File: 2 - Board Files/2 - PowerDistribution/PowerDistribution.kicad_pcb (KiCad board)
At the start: 6 copper layers, 100.1 x 100.1 mm, 64 parts, among them J201 Battery Input, J202 Battery Balance Connector, J301 Conn_02x15_Counter_Clockwise, U201 MAX40056F, U202 MAX40056F, U501 AOZ6605PI

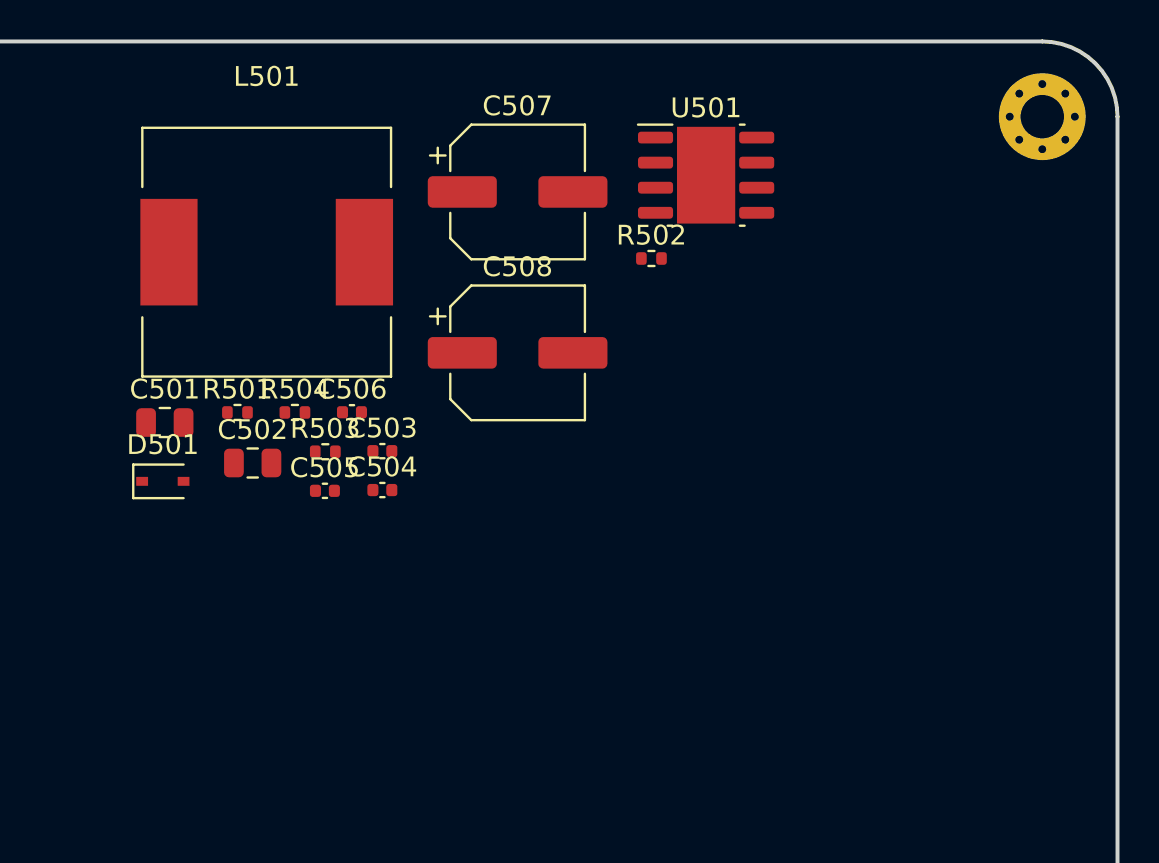
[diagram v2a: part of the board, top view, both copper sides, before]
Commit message: Switching regulator changes
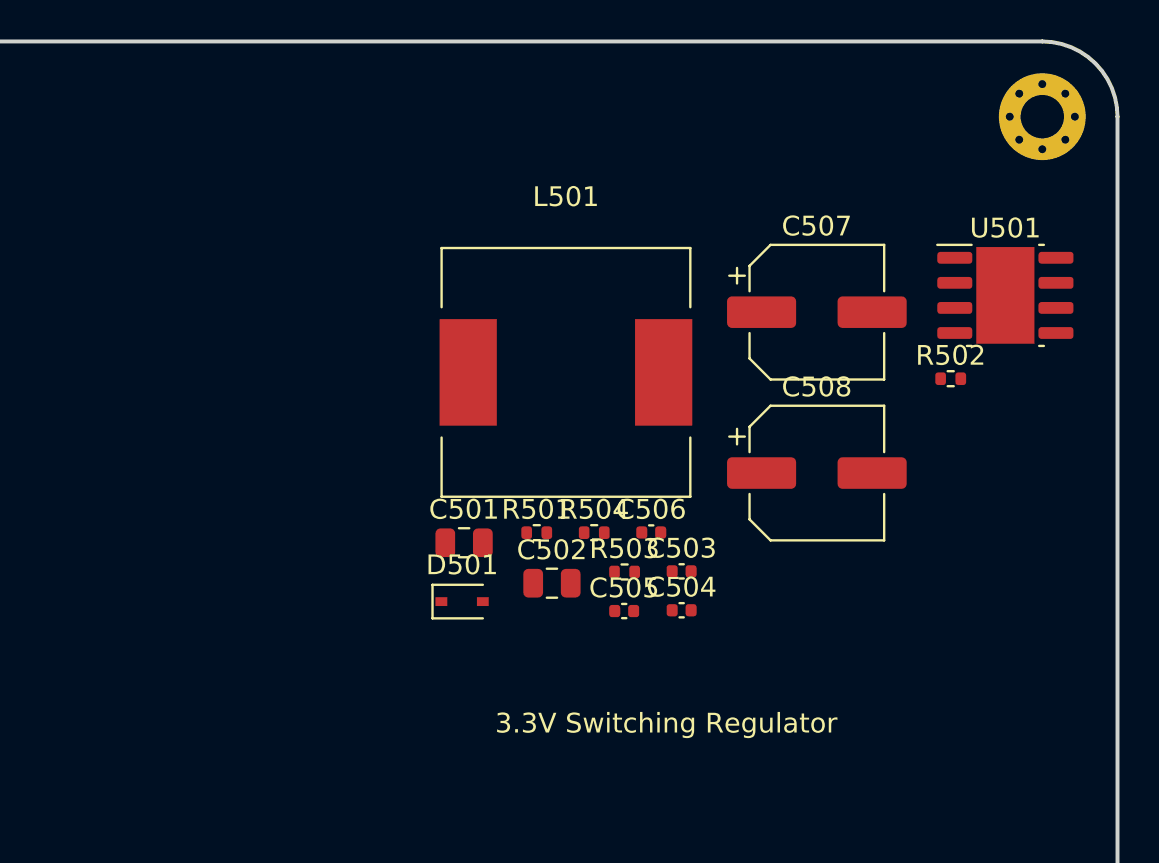
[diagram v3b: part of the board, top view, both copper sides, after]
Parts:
- moved R503 16.3 mm to (170.6, 68.5)
- moved C503 16.3 mm to (173.5, 68.5)
- moved C504 16.3 mm to (173.5, 70.5)
- moved C505 16.3 mm to (170.6, 70.5)
- moved C506 16.3 mm to (172.0, 66.5)
- moved C508 16.3 mm to (180.3, 63.5)
- moved D501 16.3 mm to (162.4, 70.0)
- moved L501 16.3 mm to (167.6, 58.4)
- moved R501 16.3 mm to (166.2, 66.5)
- moved R502 16.3 mm to (187.1, 58.7)
- moved R504 16.3 mm to (169.1, 66.5)
- moved U501 16.3 mm to (189.9, 54.5)
- moved C501 16.3 mm to (162.5, 67.0)
- moved C502 16.3 mm to (166.9, 69.1)
- moved C507 16.3 mm to (180.3, 55.4)
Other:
- board text added: "3.3V Switching Regulator"
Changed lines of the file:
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@@
   )
   (footprint "Capacitor_SMD:C_0805_2012Metric" (layer "F.Cu")
-    (at 151.77 63.01)
+    (at 166.93 69.1)
     (descr "Capacitor SMD 0805 (2012 Metric), square (rectangular) end terminal, IPC_7351 nominal, (Body size source: IPC-SM-782 page 76, https://www.pcb-3d.com/wordpress/wp-content/uploads/ipc-sm-782a_amendment_1_and_2.pdf, https://docs.google.com/spreadsheets/d/1BsfQQcO9C6DZCsRaXUlFlo91Tg2WpOkGARC1WS5S8t0/edit?usp=sharing), generated with kicad-footprint-generator")
     (tags "capacitor")
@@
   )
   (footprint "Capacitor_SMD:C_0805_2012Metric" (layer "F.Cu")
-    (at 147.32 60.96)
+    (at 162.48 67.05)
     (descr "Capacitor SMD 0805 (2012 Metric), square (rectangular) end terminal, IPC_7351 nominal, (Body size source: IPC-SM-782 page 76, https://www.pcb-3d.com/wordpress/wp-content/uploads/ipc-sm-782a_amendment_1_and_2.pdf, https://docs.google.com/spreadsheets/d/1BsfQQcO9C6DZCsRaXUlFlo91Tg2WpOkGARC1WS5S8t0/edit?usp=sharing), generated with kicad-footprint-generator")
     (tags "capacitor")
@@
   )
   (footprint "Inductor_SMD:L_12x12mm_H4.5mm" (layer "F.Cu")
-    (at 152.48 52.33)
+    (at 167.64 58.42)
     (descr "Choke, SMD, 12x12mm 4.5mm height")
     (tags "Choke SMD")
@@
   )
   (footprint "Capacitor_SMD:CP_Elec_6.3x5.4" (layer "F.Cu")
-    (at 165.19 49.28)
+    (at 180.35 55.37)
     (descr "SMD capacitor, aluminum electrolytic, Panasonic C55, 6.3x5.4mm")
     (tags "capacitor electrolytic")
@@
   )
   (footprint "Resistor_SMD:R_0402_1005Metric" (layer "F.Cu")
-    (at 171.97 52.65)
+    (at 187.13 58.74)
     (descr "Resistor SMD 0402 (1005 Metric), square (rectangular) end terminal, IPC_7351 nominal, (Body size source: IPC-SM-782 page 72, https://www.pcb-3d.com/wordpress/wp-content/uploads/ipc-sm-782a_amendment_1_and_2.pdf), generated with kicad-footprint-generator")
     (tags "resistor")
@@
   )
   (footprint "Capacitor_SMD:C_0402_1005Metric" (layer "F.Cu")
-    (at 158.34 64.38)
+    (at 173.5 70.47)
     (descr "Capacitor SMD 0402 (1005 Metric), square (rectangular) end terminal, IPC_7351 nominal, (Body size source: IPC-SM-782 page 76, https://www.pcb-3d.com/wordpress/wp-content/uploads/ipc-sm-782a_amendment_1_and_2.pdf), generated with kicad-footprint-generator")
     (tags "capacitor")
@@
   )
   (footprint "Package_SO:SOIC-8-1EP_3.9x4.9mm_P1.27mm_EP2.95x4.9mm_Mask2.71x3.4mm" (layer "F.Cu")
-    (at 174.74 48.43)
+    (at 189.9 54.52)
     (descr "SOIC, 8 Pin (http://www.ti.com/lit/ds/symlink/lm5017.pdf#page=31), generated with kicad-footprint-generator ipc_gullwing_generator.py")
     (tags "SOIC SO")
@@
   )
   (footprint "Resistor_SMD:R_0402_1005Metric" (layer "F.Cu")
-    (at 153.91 60.45)
+    (at 169.07 66.54)
     (descr "Resistor SMD 0402 (1005 Metric), square (rectangular) end terminal, IPC_7351 nominal, (Body size source: IPC-SM-782 page 72, https://www.pcb-3d.com/wordpress/wp-content/uploads/ipc-sm-782a_amendment_1_and_2.pdf), generated with kicad-footprint-generator")
     (tags "resistor")
@@
   )
   (footprint "Diode_SMD:D_SOD-323" (layer "F.Cu")
-    (at 147.22 63.94)
+    (at 162.38 70.03)
     (descr "SOD-323")
     (tags "SOD-323")
@@
   )
   (footprint "Capacitor_SMD:C_0402_1005Metric" (layer "F.Cu")
-    (at 156.8 60.44)
+    (at 171.96 66.53)
     (descr "Capacitor SMD 0402 (1005 Metric), square (rectangular) end terminal, IPC_7351 nominal, (Body size source: IPC-SM-782 page 76, https://www.pcb-3d.com/wordpress/wp-content/uploads/ipc-sm-782a_amendment_1_and_2.pdf), generated with kicad-footprint-generator")
     (tags "capacitor")
@@
   )
   (footprint "Capacitor_SMD:C_0402_1005Metric" (layer "F.Cu")
-    (at 158.34 62.41)
+    (at 173.5 68.5)
     (descr "Capacitor SMD 0402 (1005 Metric), square (rectangular) end terminal, IPC_7351 nominal, (Body size source: IPC-SM-782 page 76, https://www.pcb-3d.com/wordpress/wp-content/uploads/ipc-sm-782a_amendment_1_and_2.pdf), generated with kicad-footprint-generator")
     (tags "capacitor")
@@
   )
   (footprint "Capacitor_SMD:CP_Elec_6.3x5.4" (layer "F.Cu")
-    (at 165.19 57.43)
+    (at 180.35 63.52)
     (descr "SMD capacitor, aluminum electrolytic, Panasonic C55, 6.3x5.4mm")
     (tags "capacitor electrolytic")
@@
   )
   (footprint "Resistor_SMD:R_0402_1005Metric" (layer "F.Cu")
-    (at 155.45 62.44)
+    (at 170.61 68.53)
     (descr "Resistor SMD 0402 (1005 Metric), square (rectangular) end terminal, IPC_7351 nominal, (Body size source: IPC-SM-782 page 72, https://www.pcb-3d.com/wordpress/wp-content/uploads/ipc-sm-782a_amendment_1_and_2.pdf), generated with kicad-footprint-generator")
     (tags "resistor")
@@
   )
   (footprint "Capacitor_SMD:C_0402_1005Metric" (layer "F.Cu")
-    (at 155.43 64.42)
+    (at 170.59 70.51)
     (descr "Capacitor SMD 0402 (1005 Metric), square (rectangular) end terminal, IPC_7351 nominal, (Body size source: IPC-SM-782 page 76, https://www.pcb-3d.com/wordpress/wp-content/uploads/ipc-sm-782a_amendment_1_and_2.pdf), generated with kicad-footprint-generator")
     (tags "capacitor")
@@
   )
   (footprint "Resistor_SMD:R_0402_1005Metric" (layer "F.Cu")
-    (at 151 60.45)
+    (at 166.16 66.54)
     (descr "Resistor SMD 0402 (1005 Metric), square (rectangular) end terminal, IPC_7351 nominal, (Body size source: IPC-SM-782 page 72, https://www.pcb-3d.com/wordpress/wp-content/uploads/ipc-sm-782a_amendment_1_and_2.pdf), generated with kicad-footprint-generator")
     (tags "resistor")
@@
     (effects (font (size 1.5 1.5) (thickness 0.3)))
   )
+  (gr_text "3.3V Switching Regulator" (at 172.72 76.2) (layer "F.SilkS")
+    (effects (font (size 1 1) (thickness 0.15)))
+  )
   (gr_text "OVC FLT" (at 112.014 68.072 270) (layer "F.SilkS")

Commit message: Motor drive initial work
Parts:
- added C219: 47u, Capacitor_SMD:CP_Elec_6.3x5.4, F.Cu at (115.3, 94.7)
- added C601: 0u1, Capacitor_SMD:C_0402_1005Metric, F.Cu at (188.5, 75.8)
- added C602: 0u1, Capacitor_SMD:C_0402_1005Metric, F.Cu at (194.2, 75.8)
- added C603: 0u1, Capacitor_SMD:C_0402_1005Metric, F.Cu at (185.7, 79.8)
- added C604: 0u1, Capacitor_SMD:C_0402_1005Metric, F.Cu at (191.4, 75.8)
- added C605: 0u1, Capacitor_SMD:C_0402_1005Metric, F.Cu at (197.1, 75.8)
- added C606: 0u1, Capacitor_SMD:C_0402_1005Metric, F.Cu at (185.2, 75.9)
- added C607: 0u1, Capacitor_SMD:C_0402_1005Metric, F.Cu at (178.9, 106.1)
- added C608: 0u1, Capacitor_SMD:C_0402_1005Metric, F.Cu at (170.3, 106.1)
- added C609: 0u1, Capacitor_SMD:C_0402_1005Metric, F.Cu at (167.4, 110.1)
- added C610: 0u1, Capacitor_SMD:C_0402_1005Metric, F.Cu at (176.1, 106.1)
- added C611: 0u1, Capacitor_SMD:C_0402_1005Metric, F.Cu at (170.3, 110.1)
- added C612: 0u1, Capacitor_SMD:C_0402_1005Metric, F.Cu at (173.2, 108.1)
- added C613: 0u1, Capacitor_SMD:C_0402_1005Metric, F.Cu at (170.3, 108.1)
- added C614: 0u1, Capacitor_SMD:C_0402_1005Metric, F.Cu at (181.8, 106.1)
- added C615: 0u1, Capacitor_SMD:C_0402_1005Metric, F.Cu at (178.9, 110.1)
- added C616: 0u1, Capacitor_SMD:C_0402_1005Metric, F.Cu at (176.0, 110.1)
- added C617: 0u1, Capacitor_SMD:C_0402_1005Metric, F.Cu at (178.9, 108.1)
- added C618: 0u1, Capacitor_SMD:C_0402_1005Metric, F.Cu at (184.7, 108.1)
- added C619: 0u1, Capacitor_SMD:C_0402_1005Metric, F.Cu at (184.7, 106.1)
- added C620: 0u1, Capacitor_SMD:C_0402_1005Metric, F.Cu at (173.2, 110.1)
- added C621: 0u1, Capacitor_SMD:C_0402_1005Metric, F.Cu at (173.2, 106.1)
- added C622: 0u1, Capacitor_SMD:C_0402_1005Metric, F.Cu at (181.8, 108.1)
- added C623: 0u1, Capacitor_SMD:C_0402_1005Metric, F.Cu at (176.1, 108.1)
- added C624: 0u1, Capacitor_SMD:C_0402_1005Metric, F.Cu at (181.8, 110.1)
- added D502: D, Diode_SMD:D_SMC, F.Cu at (141.5, 72.9)
- added D503: D, Diode_SMD:D_SMC, F.Cu at (152.3, 72.9)
- added Q601: Q_NMOS_GDS, Package_TO_SOT_SMD:Infineon_PG-HSOF-8-1, F.Cu at (198.4, 86.6)
- added Q602: Q_NMOS_GDS, Package_TO_SOT_SMD:Infineon_PG-HSOF-8-1, F.Cu at (183.5, 98.2)
- added Q603: Q_NMOS_GDS, Package_TO_SOT_SMD:Infineon_PG-HSOF-8-1, F.Cu at (168.7, 98.2)
- added Q604: Q_NMOS_GDS, Package_TO_SOT_SMD:Infineon_PG-HSOF-8-1, F.Cu at (183.5, 86.6)
- added Q605: Q_NMOS_GDS, Package_TO_SOT_SMD:Infineon_PG-HSOF-8-1, F.Cu at (198.4, 98.2)
- added Q606: Q_NMOS_GDS, Package_TO_SOT_SMD:Infineon_PG-HSOF-8-1, F.Cu at (168.7, 86.6)
- added Q607: Q_NMOS_GDS, Package_TO_SOT_SMD:Infineon_PG-HSOF-8-1, F.Cu at (139.5, 151.8)
- added Q608: Q_NMOS_GDS, Package_TO_SOT_SMD:Infineon_PG-HSOF-8-1, F.Cu at (169.2, 140.2)
- added Q609: Q_NMOS_GDS, Package_TO_SOT_SMD:Infineon_PG-HSOF-8-1, F.Cu at (169.2, 116.9)
- added Q610: Q_NMOS_GDS, Package_TO_SOT_SMD:Infineon_PG-HSOF-8-1, F.Cu at (169.2, 151.8)
- added Q611: Q_NMOS_GDS, Package_TO_SOT_SMD:Infineon_PG-HSOF-8-1, F.Cu at (198.9, 116.9)
- added Q612: Q_NMOS_GDS, Package_TO_SOT_SMD:Infineon_PG-HSOF-8-1, F.Cu at (154.3, 151.8)
- added Q613: Q_NMOS_GDS, Package_TO_SOT_SMD:Infineon_PG-HSOF-8-1, F.Cu at (198.9, 140.2)
- added Q614: Q_NMOS_GDS, Package_TO_SOT_SMD:Infineon_PG-HSOF-8-1, F.Cu at (184.0, 116.9)
- added Q615: Q_NMOS_GDS, Package_TO_SOT_SMD:Infineon_PG-HSOF-8-1, F.Cu at (184.0, 151.8)
- added Q616: Q_NMOS_GDS, Package_TO_SOT_SMD:Infineon_PG-HSOF-8-1, F.Cu at (154.3, 128.5)
- added Q617: Q_NMOS_GDS, Package_TO_SOT_SMD:Infineon_PG-HSOF-8-1, F.Cu at (184.0, 128.5)
- added Q618: Q_NMOS_GDS, Package_TO_SOT_SMD:Infineon_PG-HSOF-8-1, F.Cu at (198.9, 128.5)
- added Q619: Q_NMOS_GDS, Package_TO_SOT_SMD:Infineon_PG-HSOF-8-1, F.Cu at (154.3, 140.2)
- added Q620: Q_NMOS_GDS, Package_TO_SOT_SMD:Infineon_PG-HSOF-8-1, F.Cu at (169.2, 128.5)
- added Q621: Q_NMOS_GDS, Package_TO_SOT_SMD:Infineon_PG-HSOF-8-1, F.Cu at (124.6, 151.8)
- added Q622: Q_NMOS_GDS, Package_TO_SOT_SMD:Infineon_PG-HSOF-8-1, F.Cu at (139.5, 140.2)
- added Q623: Q_NMOS_GDS, Package_TO_SOT_SMD:Infineon_PG-HSOF-8-1, F.Cu at (184.0, 140.2)
- added Q624: Q_NMOS_GDS, Package_TO_SOT_SMD:Infineon_PG-HSOF-8-1, F.Cu at (198.9, 151.8)
- added R601: 4k7, Resistor_SMD:R_0402_1005Metric, F.Cu at (188.6, 79.8)
- added R602: 4k7, Resistor_SMD:R_0402_1005Metric, F.Cu at (188.6, 77.8)
- added R603: 4k7, Resistor_SMD:R_0402_1005Metric, F.Cu at (191.5, 79.8)
- added R604: 4k7, Resistor_SMD:R_0402_1005Metric, F.Cu at (191.5, 77.8)
- added R605: 1m, 3W, Resistor_SMD:R_1206_3216Metric, F.Cu at (195.7, 79.1)
- added R606: 4k7, Resistor_SMD:R_0402_1005Metric, F.Cu at (187.6, 108.1)
- added R607: 4k7, Resistor_SMD:R_0402_1005Metric, F.Cu at (196.3, 106.8)
- added R608: 4k7, Resistor_SMD:R_0402_1005Metric, F.Cu at (184.7, 110.1)
- added R609: 4k7, Resistor_SMD:R_0402_1005Metric, F.Cu at (190.5, 106.1)
- added R610: 1m, 3W, Resistor_SMD:R_1206_3216Metric, F.Cu at (203.5, 106.1)
- added R611: 4k7, Resistor_SMD:R_0402_1005Metric, F.Cu at (193.4, 106.1)
- added R612: 4k7, Resistor_SMD:R_0402_1005Metric, F.Cu at (190.5, 110.1)
- added R613: 4k7, Resistor_SMD:R_0402_1005Metric, F.Cu at (193.6, 110.1)
- added R614: 4k7, Resistor_SMD:R_0402_1005Metric, F.Cu at (190.5, 108.1)
- added R615: 4k7, Resistor_SMD:R_0402_1005Metric, F.Cu at (187.6, 106.1)
- added R616: 4k7, Resistor_SMD:R_0402_1005Metric, F.Cu at (193.4, 108.1)
- added R617: 4k7, Resistor_SMD:R_0402_1005Metric, F.Cu at (187.6, 110.1)
- added R618: 4k7, Resistor_SMD:R_0402_1005Metric, F.Cu at (199.2, 106.8)
- added R619: 1m, 3W, Resistor_SMD:R_1206_3216Metric, F.Cu at (197.9, 109.4)
- added R620: 1m, 3W, Resistor_SMD:R_1206_3216Metric, F.Cu at (203.5, 109.4)
- added U601: BD63003MUV, Package_DFN_QFN:QFN-32-1EP_5x5mm_P0.5mm_EP3.65x3.65mm, F.Cu at (202.2, 77.2)
- added U602: BD63003MUV, Package_DFN_QFN:QFN-32-1EP_5x5mm_P0.5mm_EP3.65x3.65mm, F.Cu at (128.4, 142.4)
- added U603: BD63003MUV, Package_DFN_QFN:QFN-32-1EP_5x5mm_P0.5mm_EP3.65x3.65mm, F.Cu at (158.1, 119.1)
- added U604: BD63003MUV, Package_DFN_QFN:QFN-32-1EP_5x5mm_P0.5mm_EP3.65x3.65mm, F.Cu at (143.3, 130.7)
- C504, C506: value C_Small -> 0u1
- R501, R502: value R_Small_US -> 1k

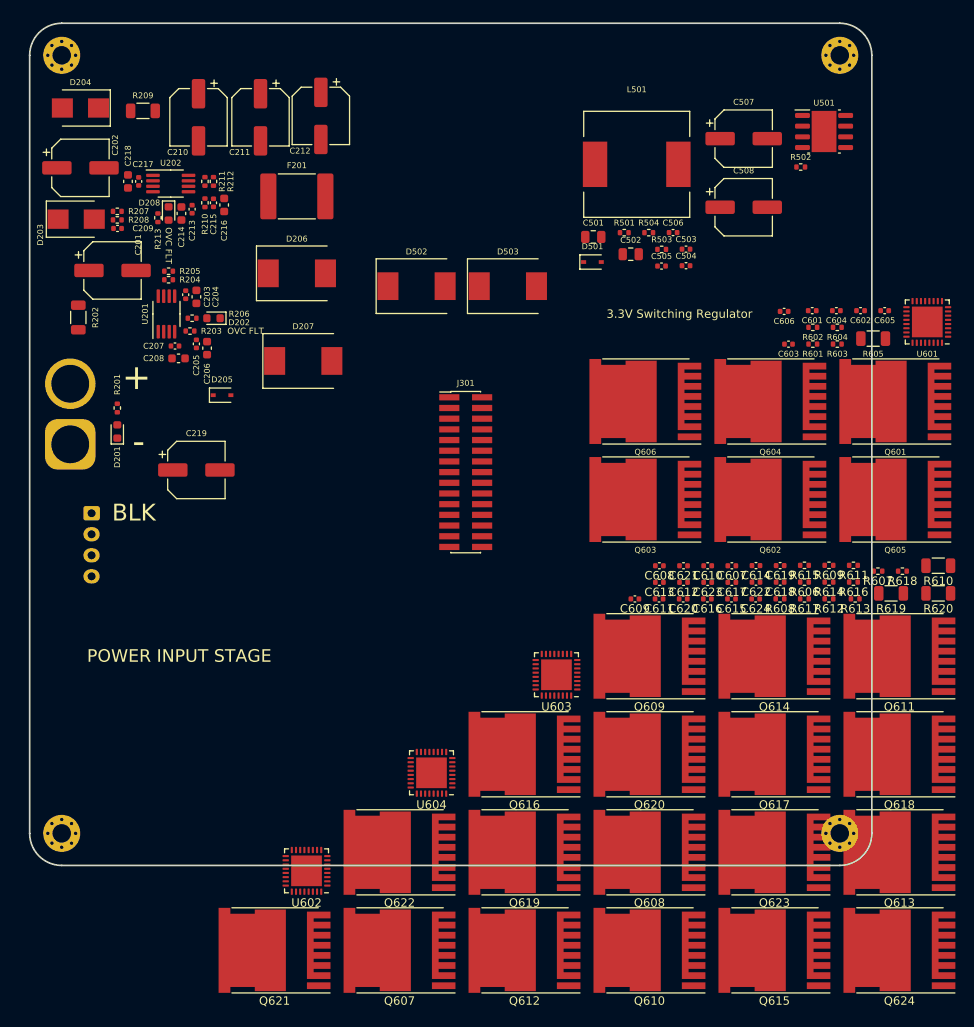
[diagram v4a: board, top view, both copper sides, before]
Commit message: MOSFETs changed
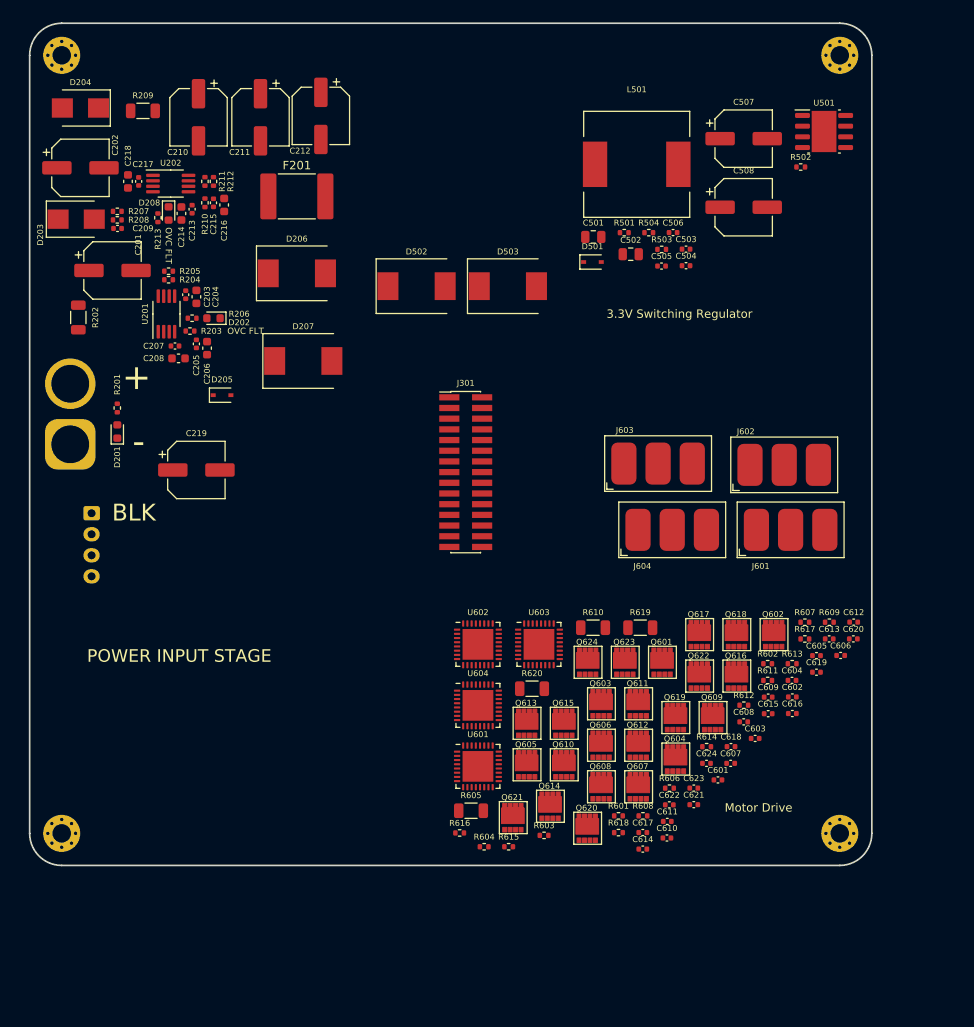
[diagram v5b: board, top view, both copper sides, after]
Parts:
- added J601: Conn_01x03_Female, QuadrotorFootprints:MotorOutputPads, F.Cu at (185.9, 101.9)
- added J602: Conn_01x03_Female, QuadrotorFootprints:MotorOutputPads, F.Cu at (185.2, 94.1)
- added J603: Conn_01x03_Female, QuadrotorFootprints:MotorOutputPads, F.Cu at (170.2, 94.0)
- added J604: Conn_01x03_Female, QuadrotorFootprints:MotorOutputPads, F.Cu at (171.9, 101.9)
- F201: footprint Fuse:Fuse_2920_7451Metric -> QuadrotorFootprints:Fuse_2920_7451Metric
- Q601, Q602, Q603, Q604, Q605, Q606, Q607, Q608, Q609, Q610, Q611, Q612, Q613, Q614, Q615, Q616, Q617, Q618, Q619, Q620, Q621, Q622, Q623, Q624: footprint Package_TO_SOT_SMD:Infineon_PG-HSOF-8-1 -> QuadrotorFootprints:8-PowerVDFN
- moved U601 75.1 mm to (148.8, 130.0), turned to 0 degrees
- moved R604 74.6 mm to (149.5, 139.5), turned to 0 degrees
- moved R605 73.7 mm to (148.0, 135.2), turned to 0 degrees
- moved R603 68.0 mm to (156.6, 138.2), turned to 0 degrees
- moved R601 60.6 mm to (165.5, 135.8), turned to 0 degrees
- moved C601 56.9 mm to (177.3, 131.6), turned to 0 degrees
- moved R616 55.5 mm to (146.6, 137.9), turned to 0 degrees
- moved Q605 54.4 mm to (153.2, 128.6), turned to 0 degrees
- moved Q624 52.2 mm to (160.5, 116.4), turned to 0 degrees
- moved R620 49.6 mm to (155.2, 120.7), turned to 0 degrees
- moved Q613 48.5 mm to (153.2, 123.7), turned to 0 degrees
- moved R615 48.5 mm to (152.4, 139.5), turned to 0 degrees
- moved C603 47.0 mm to (181.7, 126.6), turned to 0 degrees
- moved C602 46.6 mm to (186.1, 121.7), turned to 0 degrees
- moved R618 45.9 mm to (165.5, 137.8), turned to 0 degrees
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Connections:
- U602 pad 2: /MotorDrive/MOTOR1_PWM -> /MotorDrive/MOTOR2_PWM
- U602 pad 3: GND -> unconnected-(U602-Pad3)
- U603 pad 2: /MotorDrive/MOTOR1_PWM -> /MotorDrive/MOTOR3_PWM
- U604 pad 2: /MotorDrive/MOTOR1_PWM -> /MotorDrive/MOTOR4_PWM
- U604 pad 3: GND -> unconnected-(U604-Pad3)
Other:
- board text added: "Motor Drive"
